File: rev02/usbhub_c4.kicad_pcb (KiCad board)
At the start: 4 copper layers, 45.8 x 45.8 mm, 94 parts, among them J1 5077CR-16SMC2, J5 5077CR-16SMC2, J6 5077CR-16SMC2, J7 5077CR-16SMC2, J8 5077CR-16SMC2, SW1 SKRPACE010, U1 TC7SH00FU, U2 μPD720115, U3 TPS25821, U4 TPS25821, U5 TPS25821, U6 TPS25821, U7 TC7SH00FU, U8 TC7SH00FU, U9 TC7SH00FU, Y1 24MHz

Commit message: ダウンストリームポートキャパシタを高分子コンデンサに変更
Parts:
- added J2: Conn_01x02, Connector_JST:JST_PH_B2B-PH-K_1x02_P2.00mm_Vertical, F.Cu at (111.8, 80.6)
- added R10: 15kΩ, Resistor_SMD:R_0603_1608Metric, F.Cu at (107.8, 92.5)
- added R11: 10kΩ, Resistor_SMD:R_0603_1608Metric, F.Cu at (107.8, 90.8)
- added R19: 10kΩ, Resistor_SMD:R_0603_1608Metric, F.Cu at (107.8, 89.2)
- added R20: 15kΩ, Resistor_SMD:R_0603_1608Metric, F.Cu at (107.8, 87.7)
- D12: renamed from D13; value WarmWhite -> Aqua
- D13: renamed from D15; value WarmWhite -> Aqua
- D8: renamed from D9; value WarmWhite -> Aqua
- D9: renamed from D11; value WarmWhite -> Aqua
- U1: renamed from U2; footprint Package_DFN_QFN:QFN-40-1EP_6x6mm_P0.5mm_EP4.6x4.6mm -> _platinumegg:QFN-40-1EP_6x6mm_P0.5mm_EP4.6x4.6mm
- moved C9 1.32 mm to (106.1, 99.1)
- moved C12 1.09 mm to (107.1, 98.1)
- moved FB1 1.08 mm to (107.2, 95.8)
- moved C11 0.20 mm to (103.5, 94.6)
- moved R8 0.20 mm to (102.5, 94.6)
- renumbered C5 to C1, C11 to C10, C12 to C11, C13 to C12, C22 to C13, C23 to C14, C20 to C15, C25 to C16, C21 to C17, C26 to C18, C24 to C19, C6 to C2, C27 to C20, C30 to C21, C35 to C22, C31 to C23, C36 to C24, C7 to C3, C8 to C4, C14 to C5, C9 to C6, C15 to C7, C10 to C8, C16 to C9, D12 to D11, D16 to D15, D4 to D2, D5 to D3, D6 to D4, D2 to D5, D7 to D6, D8 to D7, J5 to J3, J6 to J4, J7 to J5, J8 to J6, R5 to R1, R8 to R12, R12 to R13, R16 to R14, R3 to R15, R9 to R16, R13 to R17, R17 to R18, R1 to R2, R10 to R22, R14 to R23, R18 to R24, R21 to R25, R23 to R27, R24 to R29, R2 to R3, R29 to R30, R25 to R31, R30 to R32, R31 to R33, R36 to R34, R33 to R35, R38 to R36, R34 to R37, R39 to R38, R35 to R39, R20 to R4, R6 to R5, R7 to R6, R11 to R7, R15 to R8, U7 to U2, U1 to U3, U3 to U4, U4 to U5, U8 to U6, U9 to U7, U5 to U8, U6 to U9
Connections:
- U1 pad 2: /VCC_{5V} -> /LPrwM
- U1 pad 3: /VCC_{5V} -> /V_{BUS}M
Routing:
- net /VCC_{5V}: track 61.8 -> 39.4 mm, vias 10 -> 12
- net GND: track 76.7 -> 89.8 mm, vias 40 -> 44
- net /V_{BUS}M: track 0.00 -> 12.6 mm, vias 0 -> 2
- net /LPrwM: track 0.00 -> 11.0 mm, vias 0 -> 2
- net /A3V3: track 5.74 -> 7.45 mm
- net /1V0: track 51.4 -> 52.5 mm
- net /3V3: track 67.6 -> 66.8 mm
- net /D_{U}-: track 23.8 -> 24.7 mm
- net /D_{U}+: track 22.8 -> 23.6 mm
- net /~{PPON}_{3}: track 33.2 -> 33.9 mm
- net /~{RESET}: track 34.0 -> 34.6 mm
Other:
- board text added: "Reset"
- board text added: "rev 0.3.0@2025-06-12"
- board text removed: "Reset SW"
- board text removed: "rev 0.1.1@2025-05-11"

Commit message: ダウンストリームポートキャパシタをコールドになる位置に変更
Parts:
- removed C14, C19, C20: 150uF, Capacitor_THT:CP_Radial_D6.3mm_P2.50mm
- added C25: 150uF, Capacitor_THT:CP_Radial_D6.3mm_P2.50mm, F.Cu at (118.6, 111.6)
- added C26: 150uF, Capacitor_THT:CP_Radial_D6.3mm_P2.50mm, F.Cu at (81.4, 111.6)
- added C27: 150uF, Capacitor_THT:CP_Radial_D6.3mm_P2.50mm, F.Cu at (81.4, 88.0)
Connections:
- C13 pad 1: /VCC_{5V} -> /Vout_{1}
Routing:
- net /Vout_{1}: track 9.61 -> 16.8 mm
- net /Vout_{4}: track 7.21 -> 14.0 mm
- net /VCC_{5V}: track 39.4 -> 46.2 mm, vias 12 -> 16
- net /Vout_{3}: track 9.42 -> 14.7 mm
- net /Vout_{2}: track 8.17 -> 13.4 mm
- net Net-(U9-EN): track 6.40 -> 7.86 mm
- net /~{PPON}_{4}: track 18.6 -> 19.3 mm

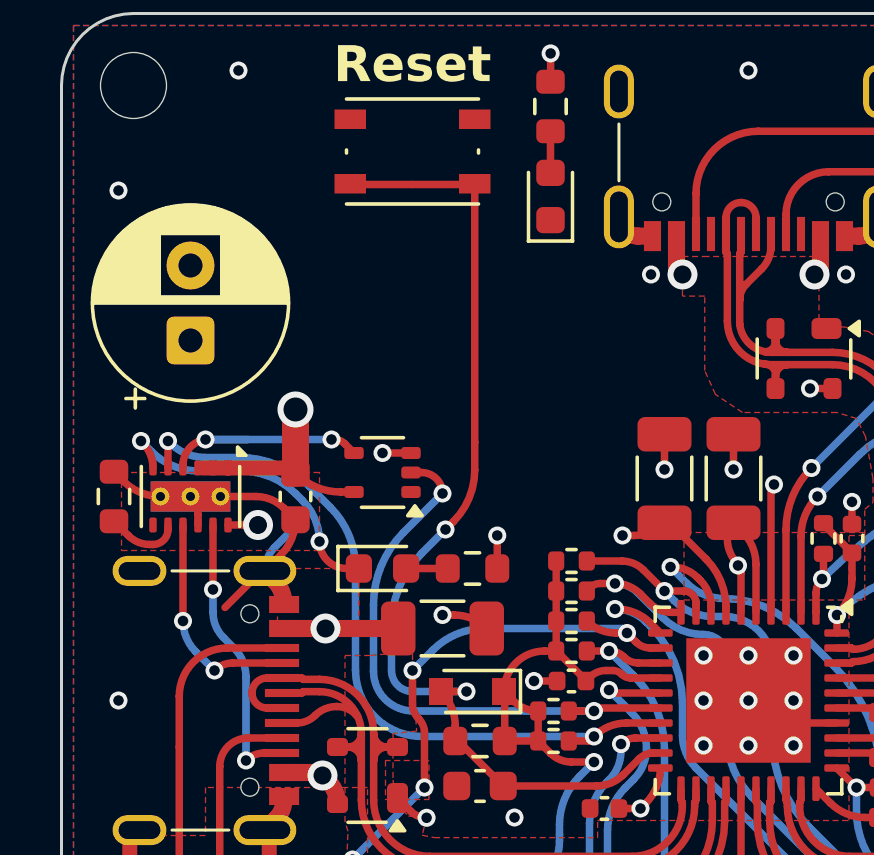
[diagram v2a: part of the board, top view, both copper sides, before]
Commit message: Add teardrops and update routing in USB hub PCB
Added teardrops to multiple pads and vias in rev02/usbhub_c4.kicad_pcb for improved manufacturability. Updated several net routings, modified some arc and segment connections, and made minor schematic and layout adjustments. Removed fabrication-toolkit-options.json files from rev01 and rev02, updated .gitignore to exclude production folders, and incremented PCB revision text to 0.3.1 with updated date.
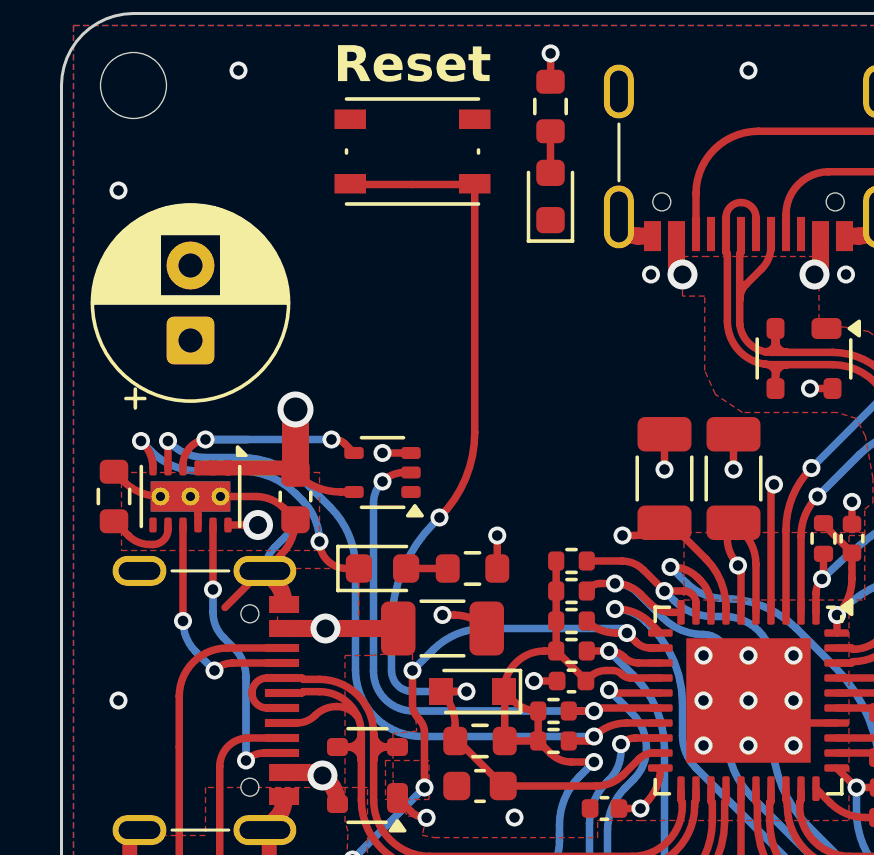
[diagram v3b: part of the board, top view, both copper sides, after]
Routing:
- net /~{PPON}_{4}: track 19.3 -> 18.6 mm
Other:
- board text added: "rev 0.3.1@2025-06-17"
- board text removed: "rev 0.3.0@2025-06-12"
